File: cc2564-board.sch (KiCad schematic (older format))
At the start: 50 parts, among them J1 TYPE-C-31-M-12, J2 Conn_ARM_JTAG_SWD_10, J3 Conn_Coaxial, J4 Conn_01x16, J5 Conn_01x16, J6 BOOT1, J7 BOOT0, SW1 SW_Push, U1 STM32F103C8Tx, U2 CC2564CRVMR, U3 LD1117#33, U4 LD1117#18, Y1 Crystal_GND24_Small

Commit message: Figure out STM32 crystal, hopefully
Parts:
- C1, C2, C8, C9: renamed from C?; footprint (none) -> Capacitor_SMD:C_0603_1608Metric_Pad1.08x0.95mm_HandSolder
- C10: renamed from C5; footprint (none) -> Capacitor_SMD:C_0603_1608Metric_Pad1.08x0.95mm_HandSolder
- C11: renamed from C6; footprint (none) -> Capacitor_SMD:C_0603_1608Metric_Pad1.08x0.95mm_HandSolder
- C12: renamed from C7; footprint (none) -> Capacitor_SMD:C_0603_1608Metric_Pad1.08x0.95mm_HandSolder
- C13: renamed from C1; footprint (none) -> Capacitor_SMD:C_0603_1608Metric_Pad1.08x0.95mm_HandSolder
- C14: renamed from C2; footprint (none) -> Capacitor_SMD:C_0603_1608Metric_Pad1.08x0.95mm_HandSolder
- C15: renamed from C3; footprint (none) -> Capacitor_SMD:C_0603_1608Metric_Pad1.08x0.95mm_HandSolder
- C16: renamed from C4; footprint (none) -> Capacitor_SMD:C_0603_1608Metric_Pad1.08x0.95mm_HandSolder
- C17: renamed from C8; value ? -> 20 pF; footprint (none) -> Capacitor_SMD:C_0603_1608Metric_Pad1.08x0.95mm_HandSolder
- C18: renamed from C9; value ? -> 20 pF; footprint (none) -> Capacitor_SMD:C_0603_1608Metric_Pad1.08x0.95mm_HandSolder
- C3: renamed from C10; footprint (none) -> Capacitor_SMD:C_0603_1608Metric_Pad1.08x0.95mm_HandSolder
- C4: renamed from C11; footprint (none) -> Capacitor_SMD:C_0603_1608Metric_Pad1.08x0.95mm_HandSolder
- C5: renamed from C12; footprint (none) -> Capacitor_SMD:C_0603_1608Metric_Pad1.08x0.95mm_HandSolder
- C6: renamed from C13; footprint (none) -> Capacitor_SMD:C_0603_1608Metric_Pad1.08x0.95mm_HandSolder
- C7: renamed from C14; footprint (none) -> Capacitor_SMD:C_0603_1608Metric_Pad1.08x0.95mm_HandSolder
- D2, D3, D5, D6: footprint (none) -> LED_SMD:LED_0603_1608Metric_Pad1.05x0.95mm_HandSolder
- D4: renamed from D1; footprint (none) -> LED_SMD:LED_0603_1608Metric_Pad1.05x0.95mm_HandSolder
- J4: renamed from J6; footprint (none) -> Connector_PinHeader_1.27mm:PinHeader_1x03_P1.27mm_Vertical
- J5: renamed from J7; footprint (none) -> Connector_PinHeader_1.27mm:PinHeader_1x03_P1.27mm_Vertical
- J6: renamed from J4; footprint (none) -> Connector_PinHeader_1.27mm:PinHeader_1x16_P1.27mm_Vertical
- J7: renamed from J5; footprint (none) -> Connector_PinHeader_1.27mm:PinHeader_1x16_P1.27mm_Vertical
- R1, R3, R4, R5, R7: renamed from R?; footprint (none) -> Resistor_SMD:R_0402_1005Metric_Pad0.72x0.64mm_HandSolder
- R10: renamed from R5; footprint (none) -> Resistor_SMD:R_0402_1005Metric_Pad0.72x0.64mm_HandSolder
- R11: renamed from R6; footprint (none) -> Resistor_SMD:R_0402_1005Metric_Pad0.72x0.64mm_HandSolder
- R12: renamed from R7; footprint (none) -> Resistor_SMD:R_0402_1005Metric_Pad0.72x0.64mm_HandSolder
- R2: renamed from R1; footprint (none) -> Resistor_SMD:R_0402_1005Metric_Pad0.72x0.64mm_HandSolder
- R6: renamed from R2; footprint (none) -> Resistor_SMD:R_0402_1005Metric_Pad0.72x0.64mm_HandSolder
- R8: renamed from R3; footprint (none) -> Resistor_SMD:R_0402_1005Metric_Pad0.72x0.64mm_HandSolder
- R9: renamed from R4; footprint (none) -> Resistor_SMD:R_0402_1005Metric_Pad0.72x0.64mm_HandSolder
- R_EXT1: value R -> 0; footprint (none) -> Resistor_SMD:R_0402_1005Metric_Pad0.72x0.64mm_HandSolder
- renumbered D4 to D1, U3 to U1, U4 to U2, U1 to U3, U2 to U4
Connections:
- no-connect marks 6 -> 7
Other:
- note added: "ECS-80-18-30-JGN-TR\n8MHz ±20ppm 18pF 100 Ohms 2-SMD\n"
- note added: "probably omit\nor solder bridge\n1 kohm if needed"
- moved on the sheet: C13, C14, C15, C16, C17, C18, J3, R_EXT1, U4A, Y1

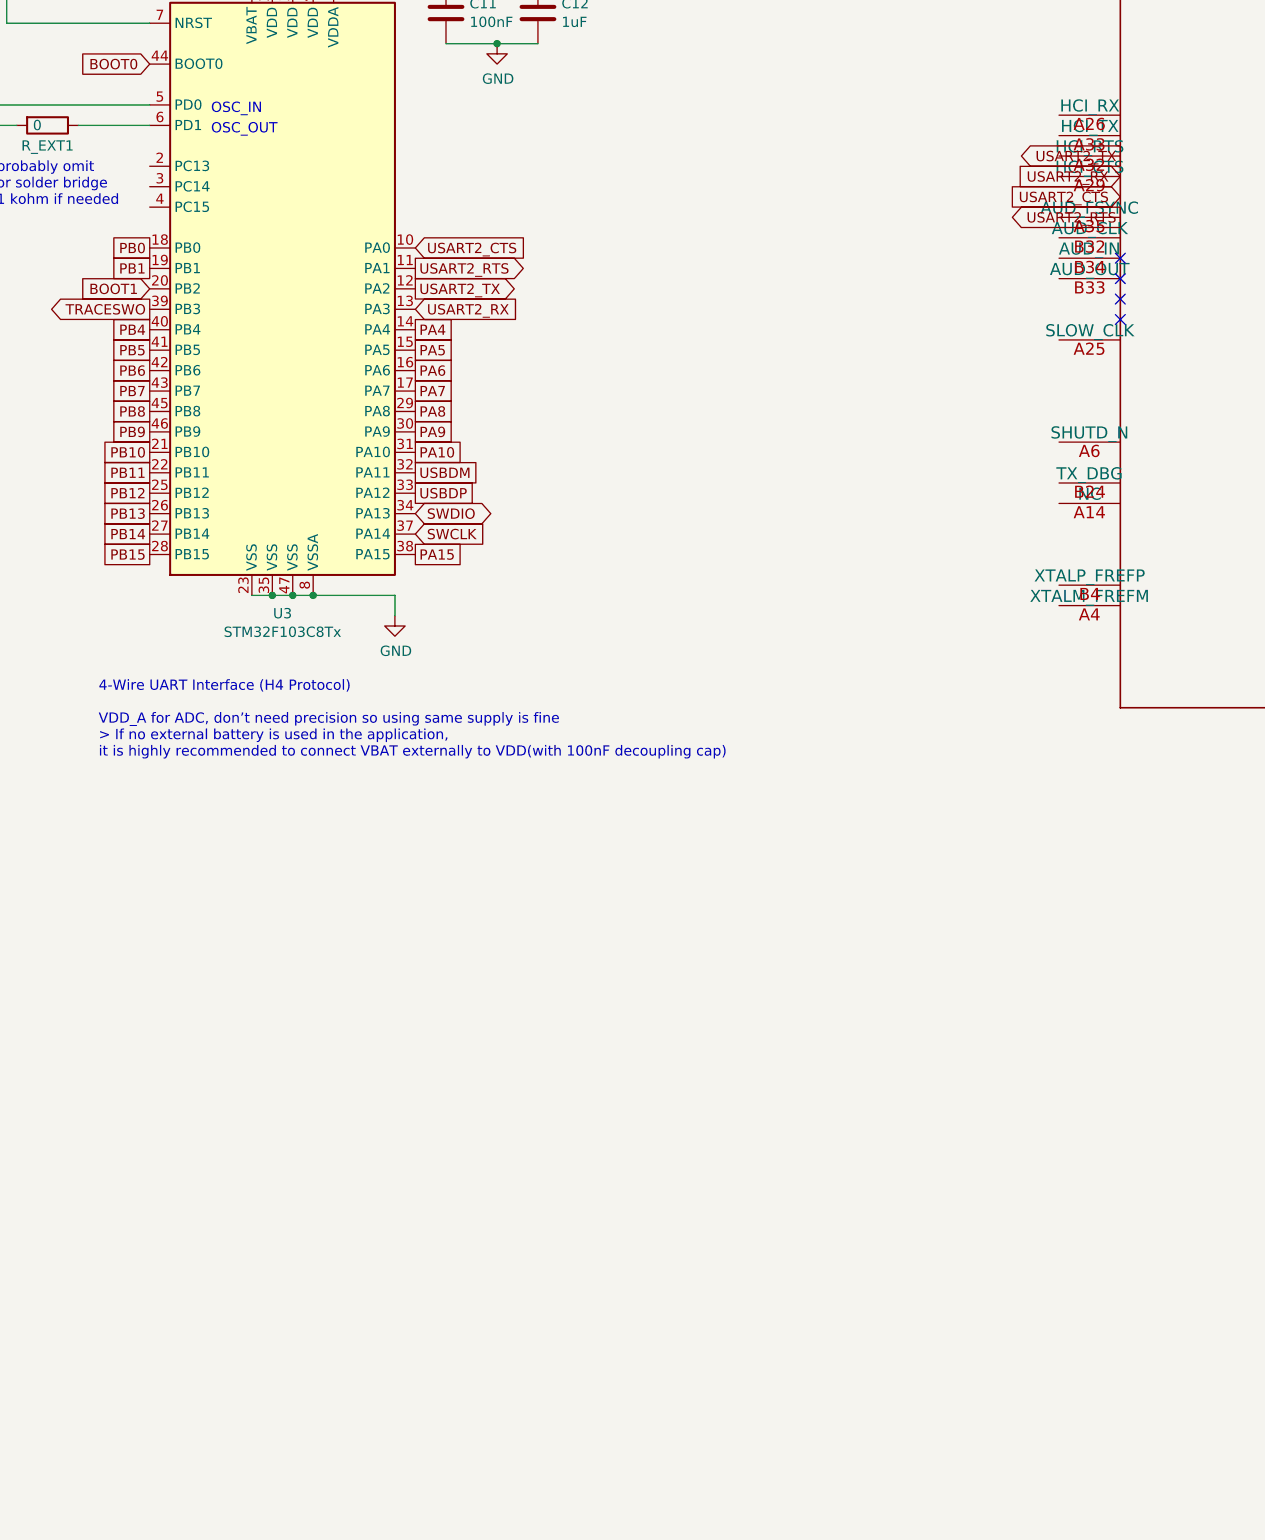
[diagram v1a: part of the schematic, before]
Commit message: Add magic TI level shifter
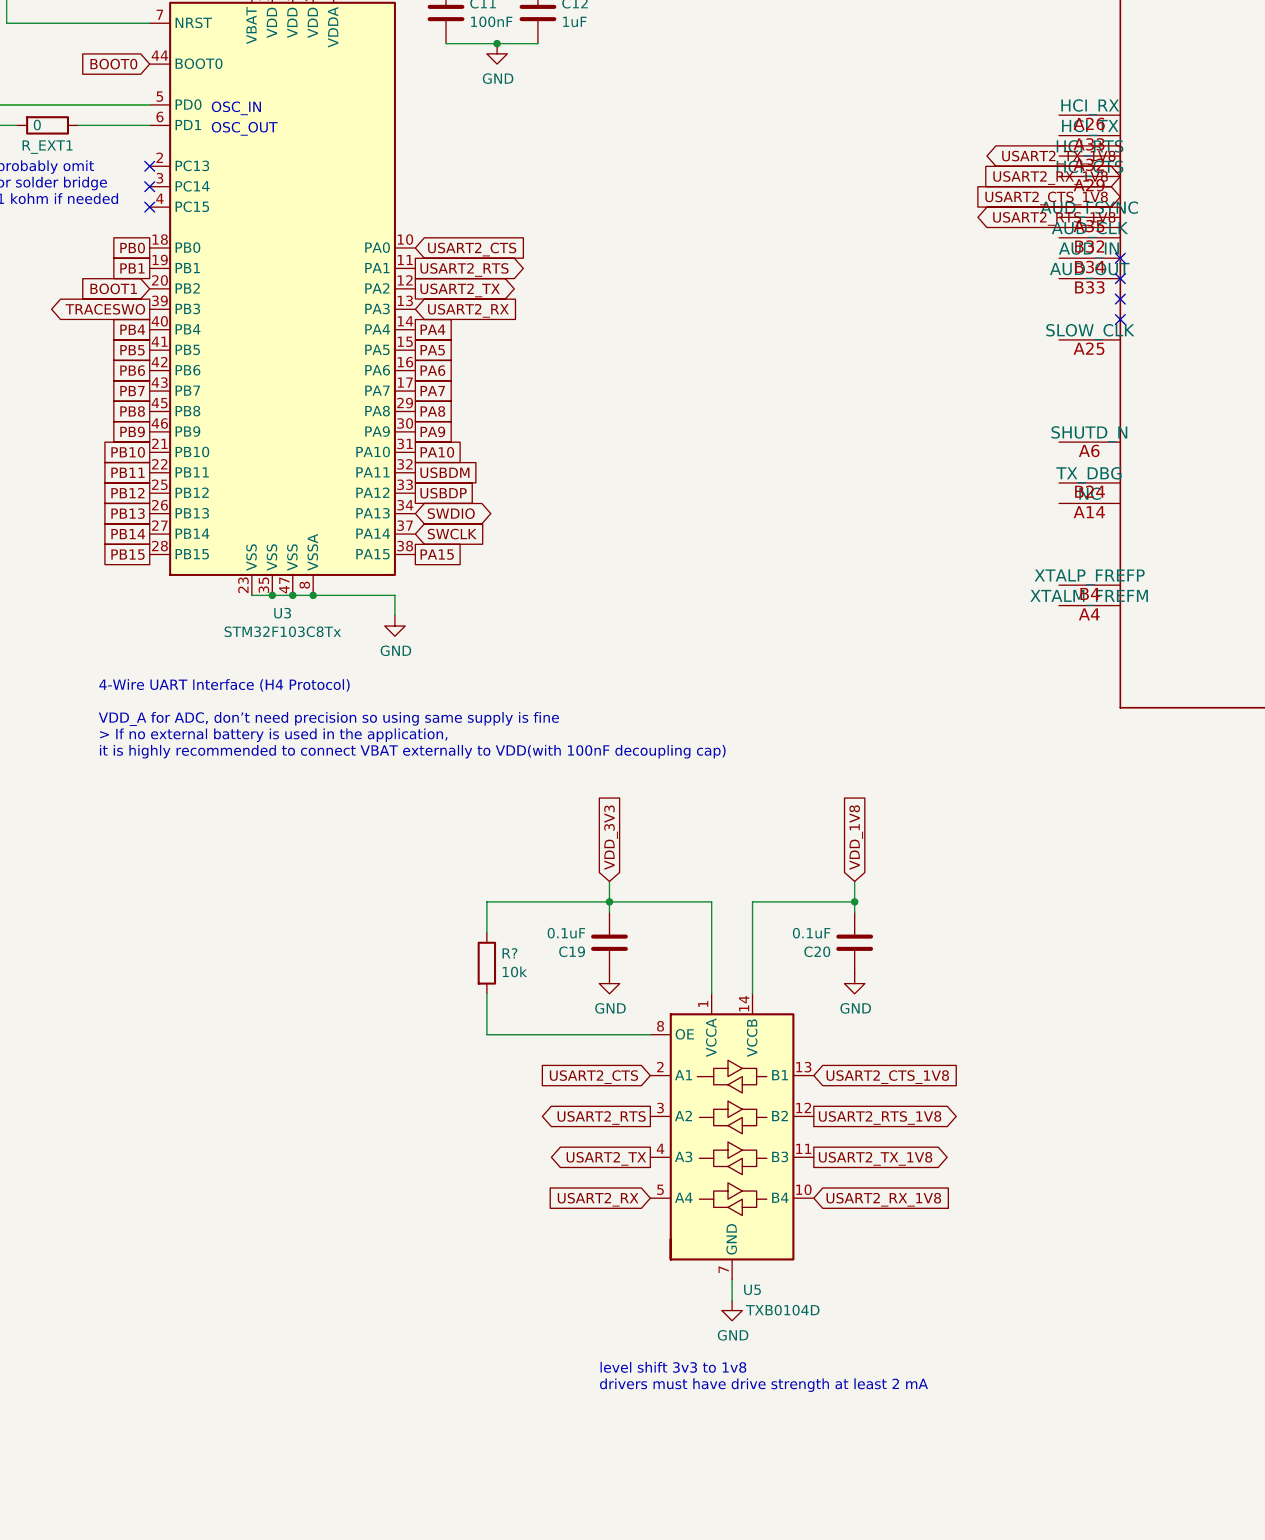
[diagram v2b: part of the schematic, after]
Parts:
- added C19, C20: 0.1uF, Capacitor_SMD:C_0603_1608Metric_Pad1.08x0.95mm_HandSolder, symbol Device:C
- added R?: 10k, symbol Device:R
- added U5: TXB0104D, Package_SO:SOIC-14_3.9x8.7mm_P1.27mm, symbol Logic_LevelTranslator:TXB0104D
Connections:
- net GND: now also C19.1, C20.1, U5.7 (GND)
- net USART2_CTS: now also U5.2 (A1)
- net USART2_RTS: now also U5.3 (A2)
- net USART2_RX: now also U5.5 (A4)
- net USART2_TX: now also U5.4 (A3)
- net VDD_1V8: now also C20.2, U5.14 (VCCB)
- net VDD_3V3: now also C19.2, R?.1, U5.1 (VCCA)
- new net: R?.2, U5.8 (OE)
- new net USART2_CTS_1V8: U5.13 (B1)
- new net USART2_RTS_1V8: U5.12 (B2)
- new net USART2_RX_1V8: U5.10 (B4)
- new net USART2_TX_1V8: U5.11 (B3)
- no-connect marks 7 -> 10
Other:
- note added: "level shift 3v3 to 1v8\ndrivers must have drive strength at least 2 mA"
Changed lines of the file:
@@
 USART2_RTS
 Text GLabel 9600 4550 0    50   Output ~ 0
-USART2_TX
+USART2_TX_1V8
 Text GLabel 9600 4650 0    50   Input ~ 0
-USART2_RX
+USART2_RX_1V8
 Text GLabel 9600 4750 0    50   Input ~ 0
-USART2_CTS
+USART2_CTS_1V8
 Text GLabel 9600 4850 0    50   Output ~ 0
-USART2_RTS
+USART2_RTS_1V8
 $Comp
 L Connector:Conn_ARM_JTAG_SWD_10 J2
@@
 	3350 4300 4850 4300
 NoConn ~ 10000 2200
+NoConn ~ 4850 4600
+NoConn ~ 4850 4700
+NoConn ~ 4850 4800
+$Comp
+L Logic_LevelTranslator:TXB0104D U5
+U 1 1 60121C0D
+P 7700 9350
+F 0 "U5" H 7800 8600 50  0000 C CNN
+F 1 "TXB0104D" H 7950 8500 50  0000 C CNN
+F 2 "Package_SO:SOIC-14_3.9x8.7mm_P1.27mm" H 7700 8600 50  0001 C CNN
+F 3 "http://www.ti.com/lit/ds/symlink/txb0104.pdf" H 7810 9445 50  0001 C CNN
+	1    7700 9350
+	1    0    0    -1
+$EndComp
+Text Notes 7050 10600 0    50   ~ 0
+level shift 3v3 to 1v8\ndrivers must have drive strength at least 2 mA
+Text GLabel 7300 9450 0    50   Output ~ 0
+USART2_TX
+Text GLabel 7300 9650 0    50   Input ~ 0
+USART2_RX
+Text GLabel 7300 9050 0    50   Input ~ 0
+USART2_CTS
+Text GLabel 7300 9250 0    50   Output ~ 0
+USART2_RTS
+$Comp
+L Device:C C19
+U 1 1 60134842
+P 7100 8400
+F 0 "C19" H 7215 8446 50  0000 L CNN
+F 1 "0.1uF" H 7215 8355 50  0000 L CNN
+F 2 "Capacitor_SMD:C_0603_1608Metric_Pad1.08x0.95mm_HandSolder" H 7138 8250 50  0001 C CNN
+F 3 "~" H 7100 8400 50  0001 C CNN
+	1    7100 8400
+	-1   0    0    1
+$EndComp
+$Comp
+L power:GND #PWR0101
+U 1 1 60135E6B
+P 7700 10150
+F 0 "#PWR0101" H 7700 9900 50  0001 C CNN
+F 1 "GND" H 7705 9977 50  0000 C CNN
+F 2 "" H 7700 10150 50  0001 C CNN
+F 3 "" H 7700 10150 50  0001 C CNN
+	1    7700 10150
+	1    0    0    -1
+$EndComp
+Wire Wire Line
+	7700 10150 7700 10050
+$Comp
+L Device:C C20
+U 1 1 6013B0A9
+P 8300 8400
+F 0 "C20" H 8415 8446 50  0000 L CNN
+F 1 "0.1uF" H 8415 8355 50  0000 L CNN
+F 2 "Capacitor_SMD:C_0603_1608Metric_Pad1.08x0.95mm_HandSolder" H 8338 8250 50  0001 C CNN
+F 3 "~" H 8300 8400 50  0001 C CNN
+	1    8300 8400
+	-1   0    0    1
+$EndComp
+Text GLabel 7100 8100 1    50   Input ~ 0
+VDD_3V3
+Text GLabel 8300 8100 1    50   Input ~ 0
+VDD_1V8
+Wire Wire Line
+	7100 8100 7100 8200
+Wire Wire Line
+	8300 8100 8300 8200
+Wire Wire Line
+	7800 8650 7800 8200
+Wire Wire Line
+	7800 8200 8300 8200
+Connection ~ 8300 8200
+Wire Wire Line
+	8300 8200 8300 8250
+Wire Wire Line
+	7600 8200 7100 8200
+Connection ~ 7100 8200
+Wire Wire Line
+	7100 8200 7100 8250
+Wire Wire Line
+	7600 8200 7600 8650
+$Comp
+L power:GND #PWR0102
+U 1 1 6015AB7F
+P 7100 8550
+F 0 "#PWR0102" H 7100 8300 50  0001 C CNN
+F 1 "GND" H 7105 8377 50  0000 C CNN
+F 2 "" H 7100 8550 50  0001 C CNN
+F 3 "" H 7100 8550 50  0001 C CNN
+	1    7100 8550
+	1    0    0    -1
+$EndComp
+$Comp
+L power:GND #PWR0103
+U 1 1 6015B046
+P 8300 8550
+F 0 "#PWR0103" H 8300 8300 50  0001 C CNN
+F 1 "GND" H 8305 8377 50  0000 C CNN
+F 2 "" H 8300 8550 50  0001 C CNN
+F 3 "" H 8300 8550 50  0001 C CNN
+	1    8300 8550
+	1    0    0    -1
+$EndComp
+Text GLabel 8100 9450 2    50   Output ~ 0
+USART2_TX_1V8
+Text GLabel 8100 9650 2    50   Input ~ 0
+USART2_RX_1V8
+Text GLabel 8100 9050 2    50   Input ~ 0
+USART2_CTS_1V8
+Text GLabel 8100 9250 2    50   Output ~ 0
+USART2_RTS_1V8
+$Comp
+L Device:R R?
+U 1 1 60186067
+P 6500 8500
+F 0 "R?" H 6570 8546 50  0000 L CNN
+F 1 "10k" H 6570 8455 50  0000 L CNN
+F 2 "" V 6430 8500 50  0001 C CNN
+F 3 "~" H 6500 8500 50  0001 C CNN
+	1    6500 8500
+	1    0    0    -1
+$EndComp
+Wire Wire Line
+	6500 8350 6500 8200
+Wire Wire Line
+	6500 8200 7100 8200
+Wire Wire Line
+	7300 8850 6500 8850
+Wire Wire Line
+	6500 8850 6500 8650
 $EndSCHEMATC

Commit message: Better CC2564 footprint, reorganize
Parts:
- removed D5, D6: LED, LED_SMD:LED_0603_1608Metric_Pad1.05x0.95mm_HandSolder, symbol Device:LED
- removed R11, R12: R, Resistor_SMD:R_0402_1005Metric_Pad0.72x0.64mm_HandSolder, symbol Device:R
- added C? (x2): 20 pF, Capacitor_SMD:C_0603_1608Metric_Pad1.08x0.95mm_HandSolder, symbol Device:C
- added unit 2 of U4
- added Y?: ECS-260-8-36CKM-TR, symbol Device:Crystal_GND24_Small
- U4: footprint cc2654-board-footprints:XCVR_CC2564CRVMR -> cc2654-board-footprints:CC2564CRVMR; MANUFACTURER Texas Instruments -> (none); MAXIMUM_PACKAGE_HEIGHT 0.9mm -> (none); PARTREV June 22, 2020 -> (none); STANDARD Manufacturer Recommendation -> (none)
- gave numbers to parts that had none: 1
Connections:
- net BOOT2 is gone; now on net BOOT0: J5.2 (Pin_2)
- net GND: now also C17.1, U4.B4 (XTALP_FREFP), C?.1, C?.1, C?.2, U4.A10 (NC), U4.A11 (NC), U4.A24 (VSS), U4.A28 (VSS), U4.B11 (VSS_DCO), U4.B3 (VSS_FREF), U4.B9 (NC), U4.D1 (EPAD), Y?.1, Y?.2, Y?.4; no longer C17.2, R_EXT1.2
- net USART2_CTS_1V8: now also U4.A32 (HCI_RTS)
- net USART2_RTS_1V8: now also U4.A29 (HCI_CTS)
- net USART2_RX_1V8: now also U4.A33 (HCI_TX)
- net USART2_TX_1V8: now also U4.A26 (HCI_RX)
- net VDD_1V8: now also U4.A17 (VDD_IO), U4.A34 (VDD_IO), U4.A38 (VDD_IO), U4.B18 (VDD_IO), U4.B19 (VDD_IO), U4.B21 (VDD_IO), U4.B22 (VDD_IO), U4.B25 (VDD_IO)
- net at U4.A4 (XTALM_FREFM): now also C?.2, Y?.3
- net TX_DBG: now reaches U4.B24 (TX_DBG)
- net at U3.5 (PD0), Y1.1: now also C17.2; no longer C17.1
- net at C18.2, Y1.3: now also R_EXT1.2
- no-connect marks 10 -> 40
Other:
- note added: "A10, A11, B9, and B10 are GND for improved RF performance"
- moved on the sheet: C13, C14, C15, C16, C17, C18, C19, C20, D2, D3, D4, J3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

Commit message: BT slow clock and other things I don't remember
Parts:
- added C?: 0.1uF, Capacitor_SMD:C_0603_1608Metric_Pad1.08x0.95mm_HandSolder, symbol Device:C
- added R?: 10k, symbol Device:R
- added Y?: ECS-327MVATX-3-CN-TR, OSC_ECS-2333-160-BN-TR, symbol ECS-327MVATX-3-CN-TR:ECS-327MVATX-3-CN-TR
- C21, C22: renamed from C?; value 20 pF -> 10 pF
- D4: value LED -> GREEN
- R3, R4: value 22 -> 0
- gave numbers to parts that had none: 1
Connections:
- net GND: now also C?.2, Y?.2 (GND)
- net USBDM: no longer J1.A7 (DN1)
- net USBDP: no longer J1.A6 (DP1)
- net VDD_1V8: now also C?.1, R?.1, Y?.4 (VDD)
- net at J1.B6 (DP2), R4.2: now also J1.A6 (DP1)
- net at J1.B7 (DN2), R3.1: now also J1.A7 (DN1)
- net BT_SLOW_CLK: now reaches U4.A25 (SLOW_CLK)
- net BT_SLOW_CLK: now also Y?.3 (OUTPUT)
- new net: R?.2, Y?.1 (TRI-STATE)
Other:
- note added: "consider enable from stm32 gpio"
- note added: "stm32 shouldn’t need serial termination resistors\n22ohm if needed"
- moved on the sheet: C1, C10, C11, C12, C17, C18, C2, C8, C9, D1, D2, D3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

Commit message: LEDs, maybe
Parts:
- added R13: 0, symbol Device:R
- D4: value GREEN -> GREEN 150060GS75000
- R10: value R -> 90
- R8: value R -> 55
- R9: value R -> 4
- gave numbers to parts that had none: 3
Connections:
- net BT_SLOW_CLK: now also R13.1; no longer Y3.3 (OUTPUT)
- net BT_AUD_FSYNC: now reaches U4.A35 (AUD_FSYNC)
- net BT_AUD_CLK: now reaches U4.B32 (AUD_CLK)
- net BT_AUD_OUT: now reaches U4.B33 (AUD_OUT)
- net BT_AUD_IN: now reaches U4.B34 (AUD_IN)
- net TX_DBG renamed BT_TX_DBG
- net USBDM renamed USB_D-
- net USBDP renamed USB_D+
- new net: R13.2, Y3.3 (OUTPUT)
- no-connect marks 40 -> 36
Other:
- note added: "350-2436-1-ND‎"
- moved on the sheet: C13, C14, C15, C16, C19, C20, C21, C22, C23, J3, J4, J5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
